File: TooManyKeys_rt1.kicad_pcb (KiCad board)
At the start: 6 copper layers, 156 x 116.5 mm, 89 parts, among them U1 TLV61070ADBV, U2 SN74LV1T126DBVR

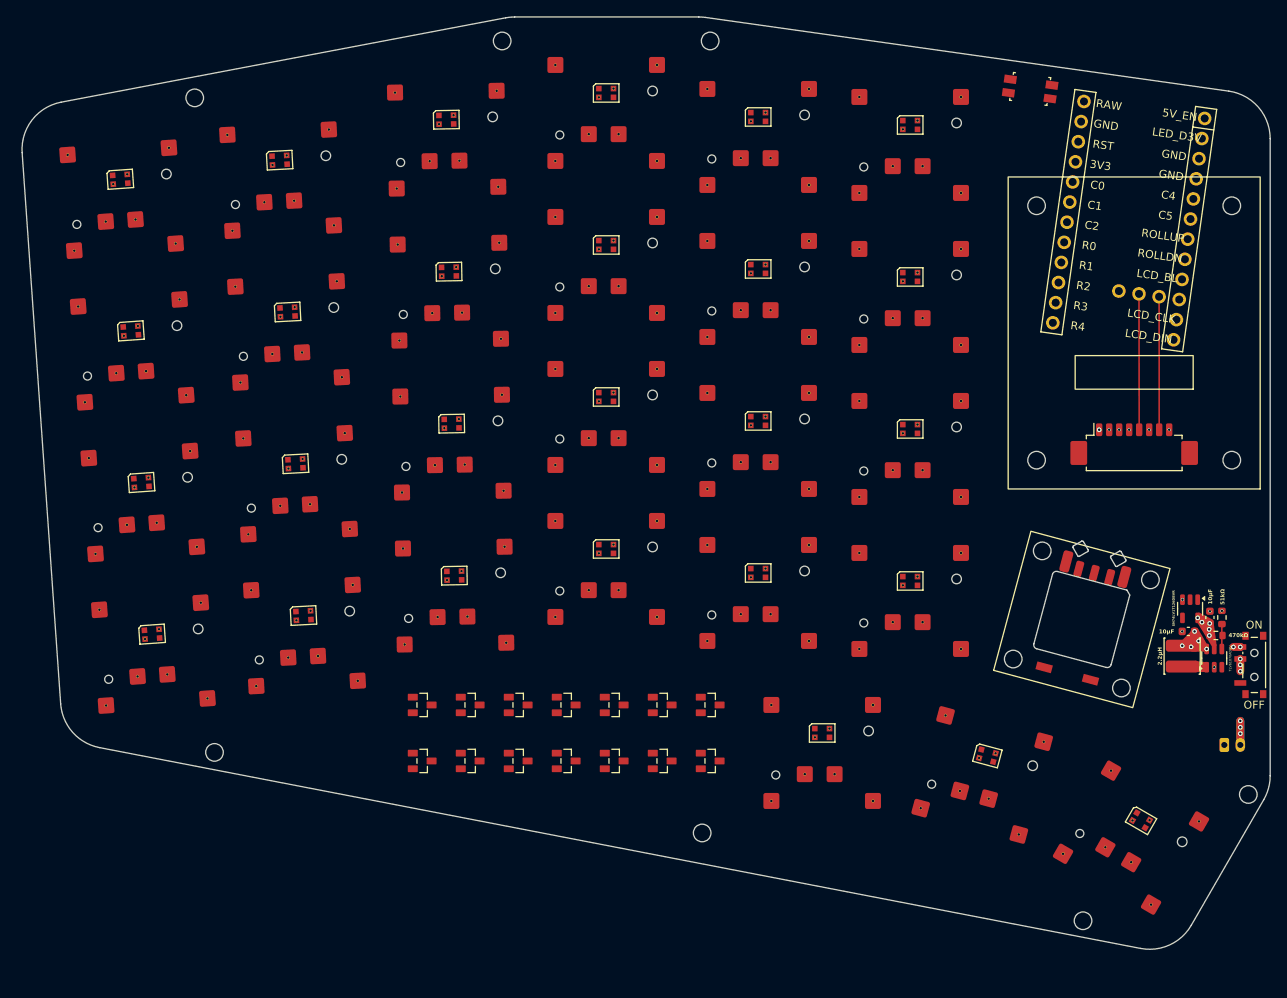
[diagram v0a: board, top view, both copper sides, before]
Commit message: Finish clean routing. Attempted sync of schematic failed, but board LGTM and passes DRC other than CKW12 edge issues of no concern.
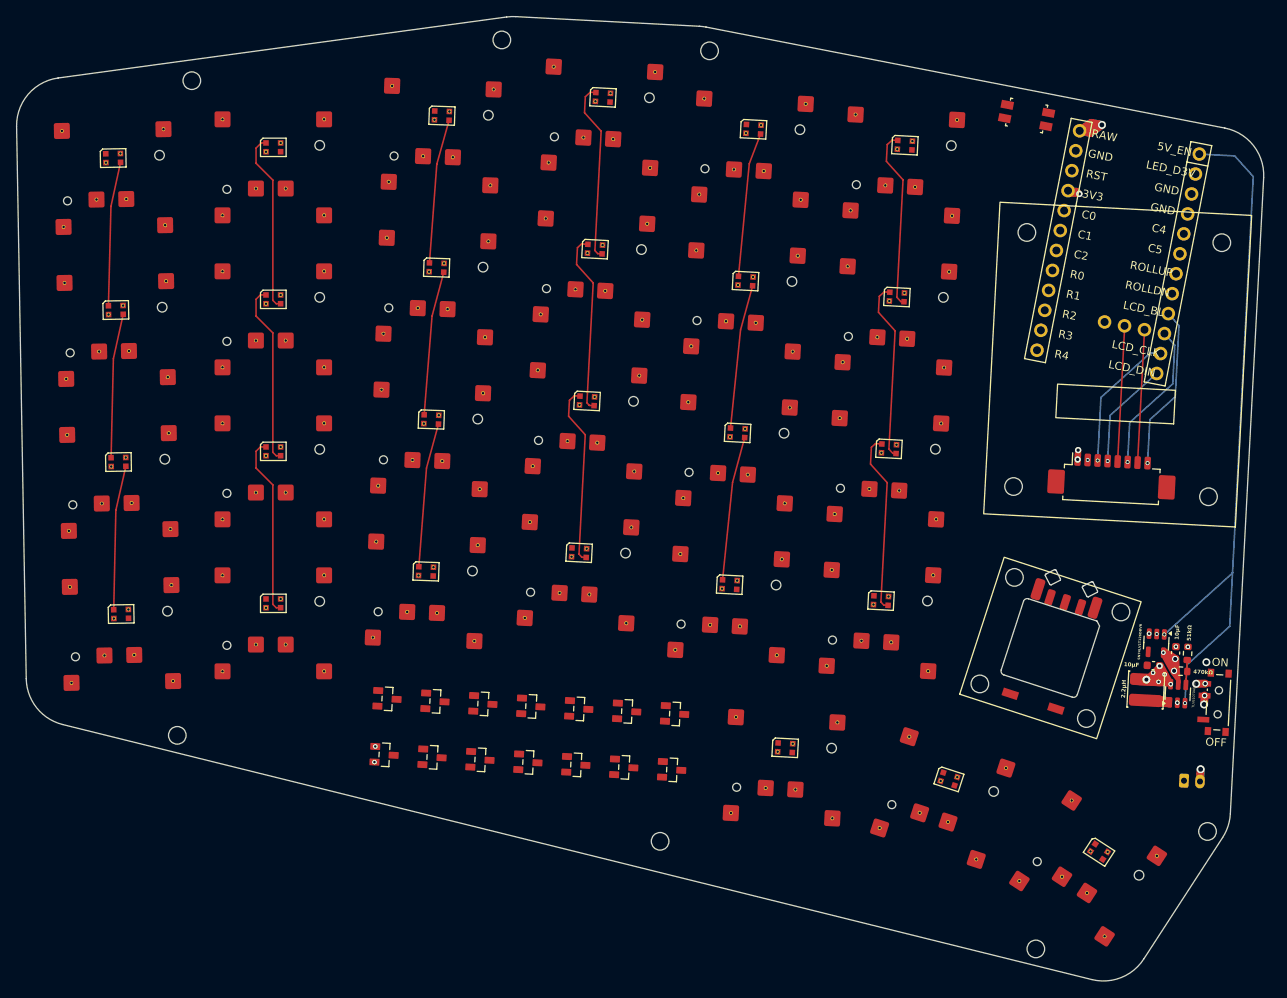
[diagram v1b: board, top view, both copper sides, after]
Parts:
- moved MH7 6.89 mm to (192.4, 182.2), turned to -33 degrees
- moved MH6 6.87 mm to (171.0, 196.9), turned to -33 degrees
- moved JST1 6.77 mm to (190.5, 175.9), turned to 177 degrees
- moved S27 6.60 mm to (177.5, 186.8), turned to -33 degrees
- moved LED27 6.55 mm to (178.9, 184.7), turned to -33 degrees
- moved PWR1 6.49 mm to (193.8, 166.1), turned to -3 degrees
- moved U1 6.36 mm to (188.7, 165.0), turned to 87 degrees
- moved R1 6.27 mm to (189.1, 162.2), turned to -3 degrees
- moved R2 6.22 mm to (189.9, 160.0), turned to 87 degrees
- moved L1 6.21 mm to (184.7, 164.5), turned to -93 degrees
- moved C2 6.16 mm to (188.4, 159.9), turned to 87 degrees
- moved C1 6.12 mm to (185.7, 161.5), turned to 177 degrees
- moved U2 6.03 mm to (186.0, 158.7), turned to -93 degrees
- moved S26 5.71 mm to (159.3, 178.0), turned to -18 degrees
- moved LED26 5.62 mm to (160.1, 175.7), turned to -18 degrees
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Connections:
- D12 pad 1: finger_inner_bottom -> finger_index_bottom
- D12 pad 2: finger_index_bottom -> finger_inner_bottom
- D2 pad 1: finger_middle_num -> finger_ring_num
- D2 pad 2: finger_ring_num -> finger_middle_num
- D3 pad 1: finger_inner_num -> finger_index_num
- D3 pad 2: finger_index_num -> finger_inner_num
- D5 pad 1: finger_middle_top -> finger_ring_top
- D5 pad 2: finger_ring_top -> finger_middle_top
- D6 pad 1: finger_inner_top -> finger_index_top
- D6 pad 2: finger_index_top -> finger_inner_top
- D8 pad 1: finger_middle_home -> finger_ring_home
- D8 pad 2: finger_ring_home -> finger_middle_home
- D9 pad 1: finger_inner_home -> finger_index_home
- D9 pad 2: finger_index_home -> finger_inner_home
- MCU1 pad 11: LCD_CLK -> LCD_DIN
- MCU1 pad 12: LCD_DIN -> LCD_CLK
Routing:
- net RAW: track 108.8 -> 264.4 mm, vias 7 -> 10
- net 5V_EN: track 0.00 -> 87.7 mm, vias 0 -> 2
- net 3V3: track 35.2 -> 79.8 mm, vias 1 -> 3
- net LED_13: track 0.00 -> 22.8 mm
- net LED_4: track 0.00 -> 22.7 mm
- net LED_12: track 0.00 -> 22.7 mm
- net LED_14: track 0.00 -> 22.7 mm
- net LED_21: track 0.00 -> 22.6 mm
- net LED_20: track 0.00 -> 22.6 mm
- net LED_5: track 0.00 -> 22.6 mm
- net LED_6: track 0.00 -> 22.6 mm
- net LED_22: track 0.00 -> 22.6 mm
- net LED_8: track 0.00 -> 18.1 mm
- net LED_26: track 0.00 -> 18.1 mm
- net LED_16: track 0.00 -> 18.1 mm
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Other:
- board size 156 x 116.5 mm -> 155.9 x 120.5 mm
